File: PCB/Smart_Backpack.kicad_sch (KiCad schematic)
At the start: 16 parts, among them SW1 SW_Push_Dual_x2, U3 ESP32-PICO-MINI-02-N8R2

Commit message: lots of 'final' schematic updates. ERC is essentially clean, PCB design can begin
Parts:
- removed SW1: SW_Push_Dual_x2, SMD_Button:Shop_SMD_Button, symbol Switch:SW_Push_Dual_x2
- added SW1: SW_Push, SMD_Button:Shop_SMD_Button, symbol Switch:SW_Push
- C12, C13: value C -> 15pF; footprint (none) -> Capacitor_SMD:C_1206_3216Metric_Pad1.33x1.80mm_HandSolder
- R18: value R_US -> 10MΩ; footprint (none) -> Resistor_SMD:R_1206_3216Metric_Pad1.30x1.75mm_HandSolder
- RTC1: renamed from RTC; footprint (none) -> RTC:XTAL_AB38T-32.768KHZ-B7
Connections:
- net GND: now also SW1.1
- net MOIST_SIG: now reaches U3.10 (I35)
- net LAPTOP: now reaches U3.15 (IO25)
- net RFID_RST: now reaches U3.17 (IO27)
- net HALL_1: now reaches U3.4 (I36)
- net HALL_2: now reaches U3.5 (I37)
- net FLEX_1: now reaches U3.6 (I38)
- net FLEX_2: now reaches U3.7 (I39)
- net at C9.1, R11.1: now also SW1.2
- no-connect marks 1 -> 7

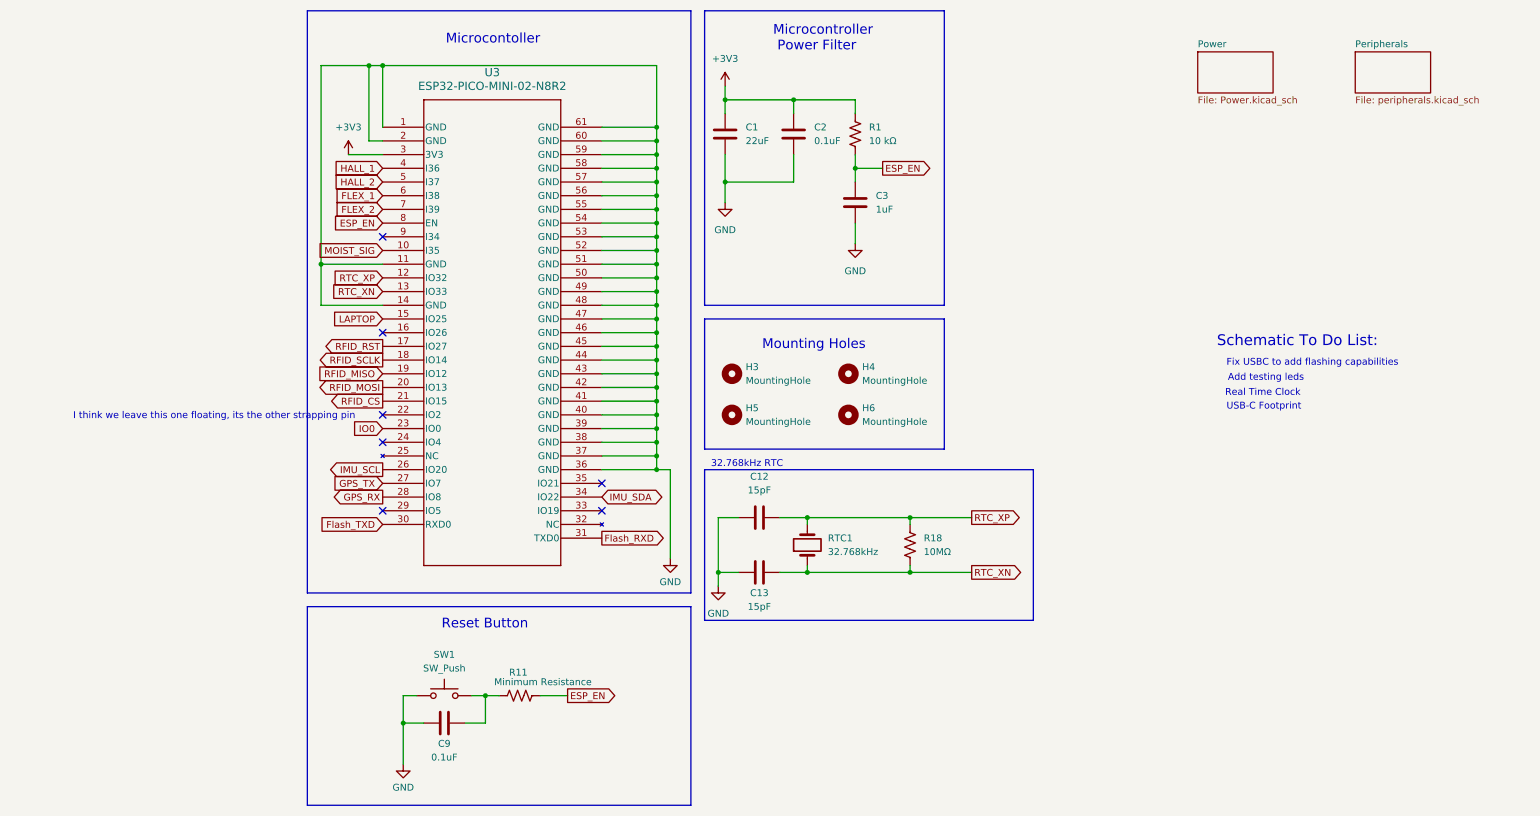
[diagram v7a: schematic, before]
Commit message: Created BOM and added USBC footprint
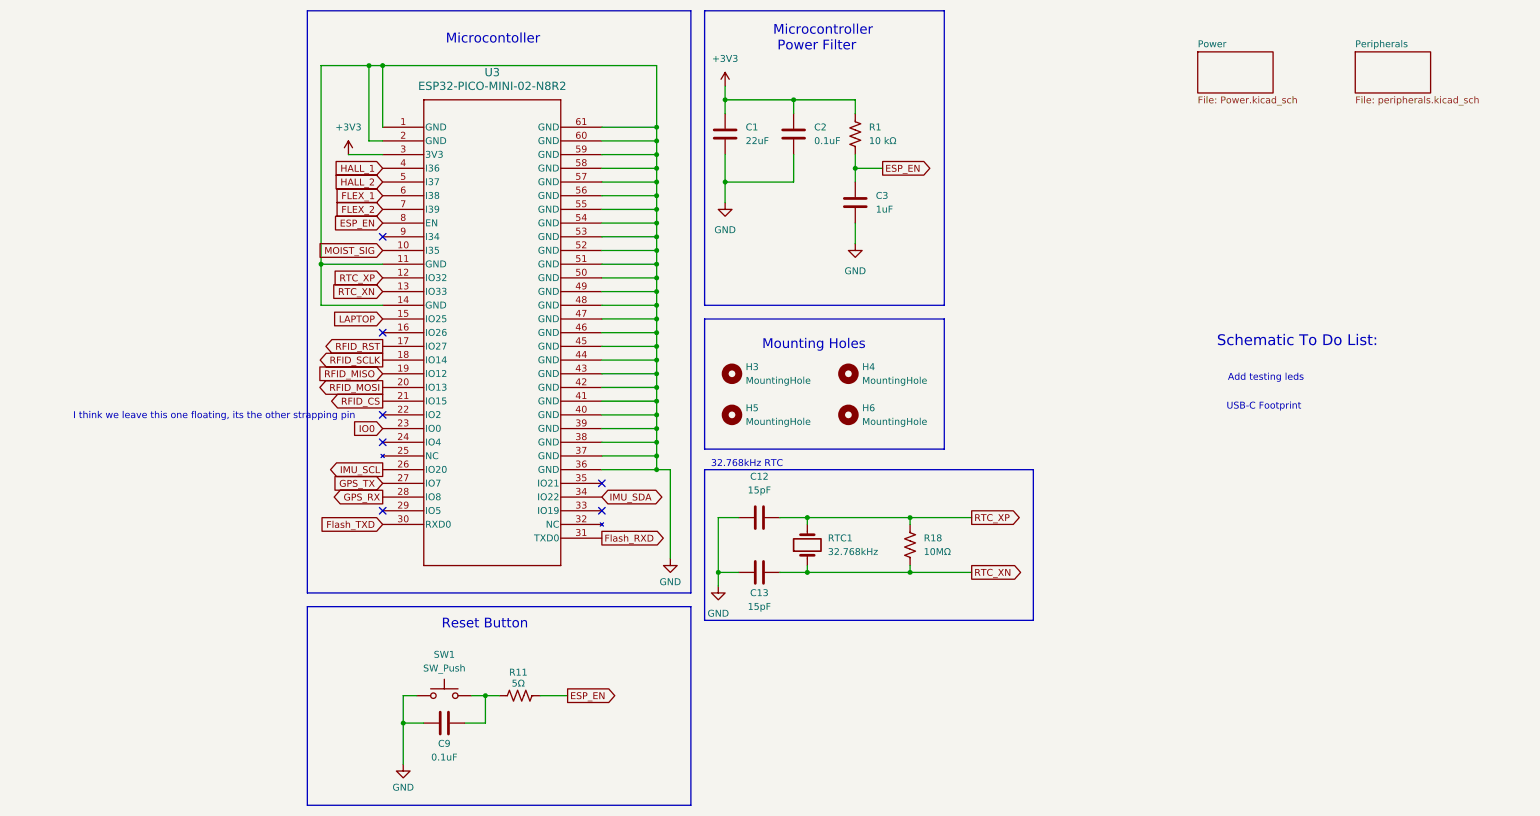
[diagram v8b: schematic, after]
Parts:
- R11: value Minimum Resistance -> 5Ω
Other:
- note removed: "Fix USBC to add flashing capabilities"
- note removed: "Real Time Clock"
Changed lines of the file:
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@@
 		)
 	)
-	(text "Real Time Clock"
-		(exclude_from_sim no)
-		(at 184.15 85.598 0)
-		(effects
-			(font
-				(size 1.27 1.27)
-			)
-			(justify left bottom)
-		)
-	)
 	(text "Microcontoller\n"
 		(exclude_from_sim no)
@@
 		)
 	)
-	(text "Fix USBC to add flashing capabilities\n"
-		(exclude_from_sim no)
-		(at 184.404 80.01 0)
-		(effects
-			(font
-				(size 1.27 1.27)
-			)
-			(justify left bottom)
-		)
-	)
 	(text "Add testing leds"
 		(exclude_from_sim no)
@@
 			)
 		)
-		(property "Value" "Minimum Resistance"
-			(at 57.658 138.43 90)
+		(property "Value" "5Ω"
+			(at 53.086 138.684 90)
 			(effects
 				(font
